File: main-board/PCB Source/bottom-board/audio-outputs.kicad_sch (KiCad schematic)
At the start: 53 parts, among them P11 JACK_TRS_6PINS, P12 JACK_TRS_6PINS, U6 OPA1678IDR, U7 OPA1678IDR

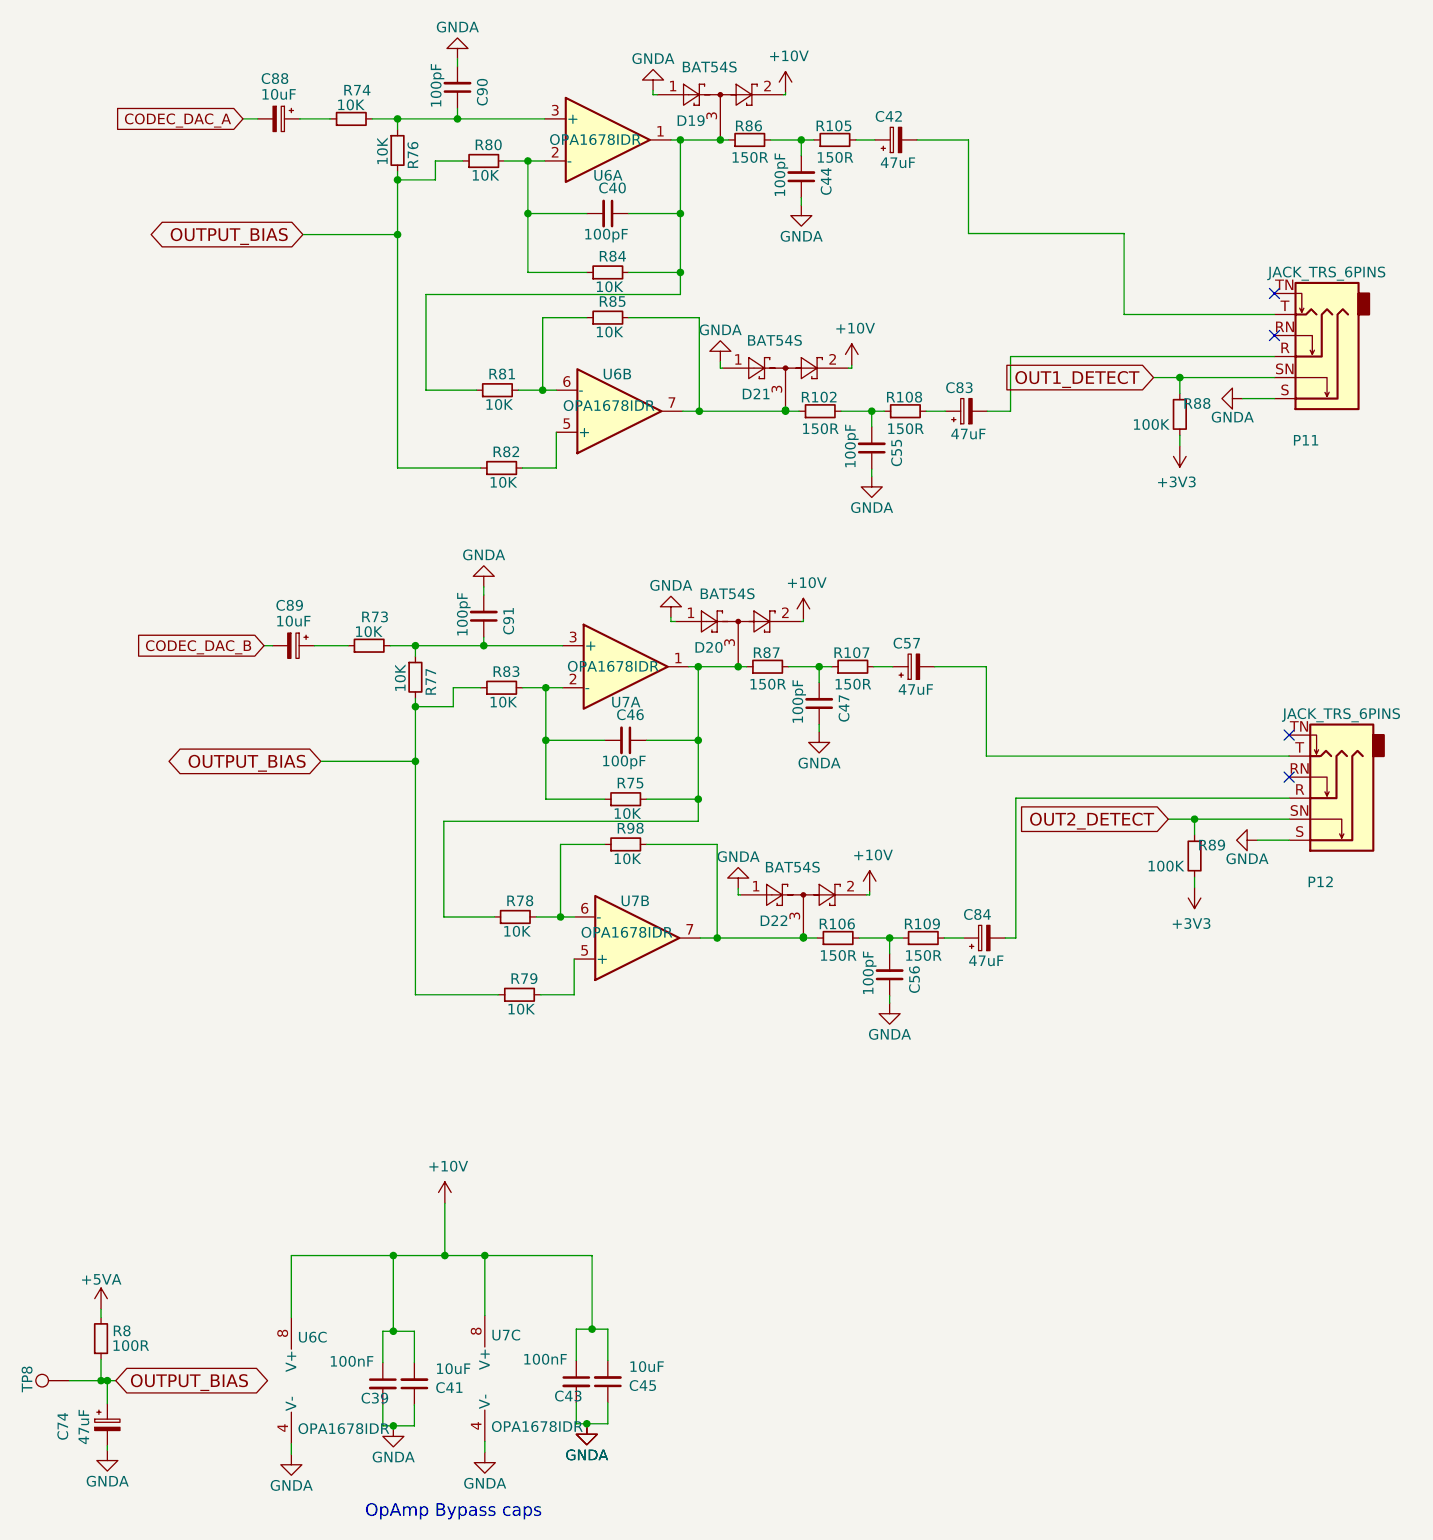
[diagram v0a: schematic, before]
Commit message: mainboard: add bias buffer, update MPNs, clean schematic
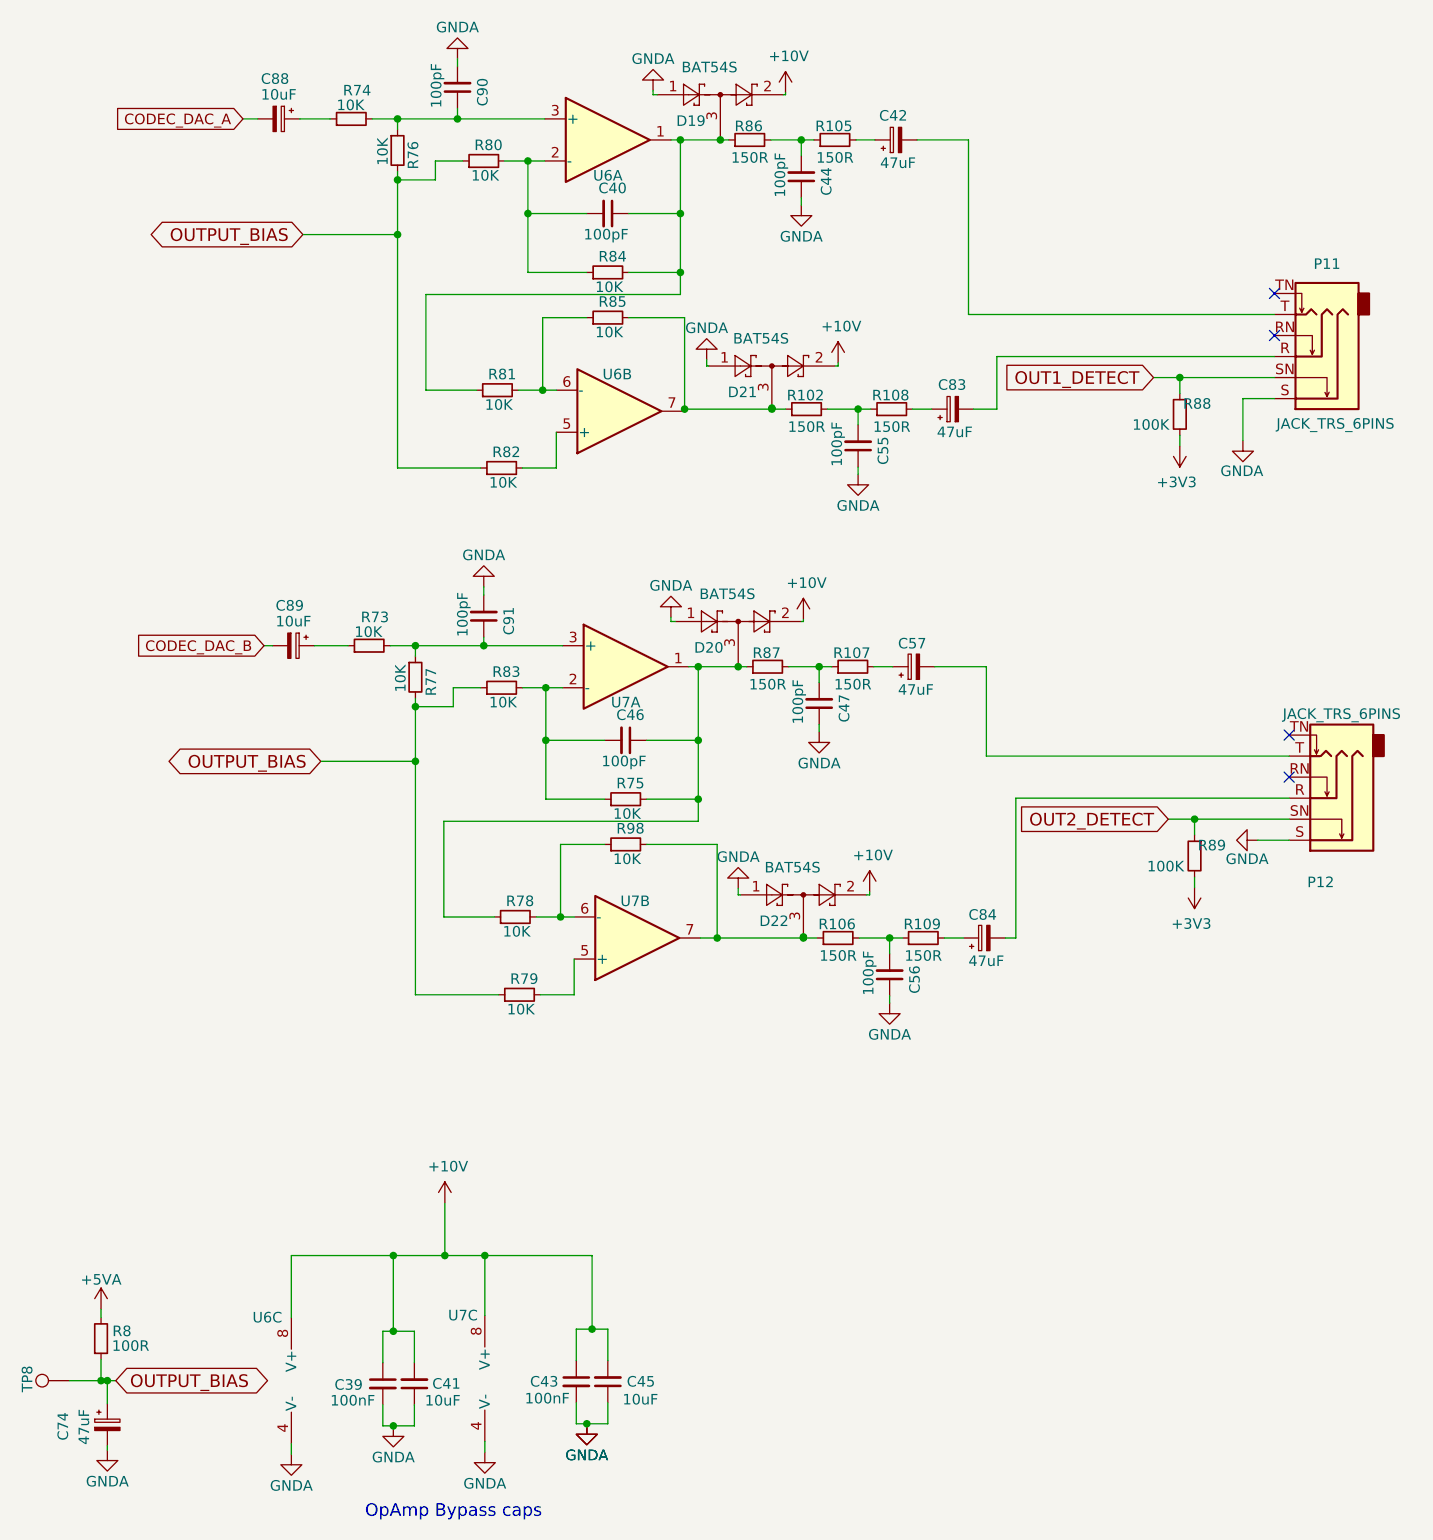
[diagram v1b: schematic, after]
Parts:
- U6, U7: value OPA1678IDR -> (none); footprint Package_SO:SOIC-8_3.9x4.9mm_P1.27mm -> (none)
- U6: value OPA1678IDR -> (none); footprint Package_SO:SOIC-8_3.9x4.9mm_P1.27mm -> (none); MPN (none) -> OPA1678IDR
- U6, U7: value OPA1678IDR -> (none); footprint Package_SO:SOIC-8_3.9x4.9mm_P1.27mm -> (none); MPN LM833DT -> OPA1678IDR
- U7: value OPA1678IDR -> (none); footprint Package_SO:SOIC-8_3.9x4.9mm_P1.27mm -> (none); MPN TL082CDR -> OPA1678IDR
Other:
- moved on the sheet: C55, C83, D21, R102, R108

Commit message: mainboard: modify silkscreen
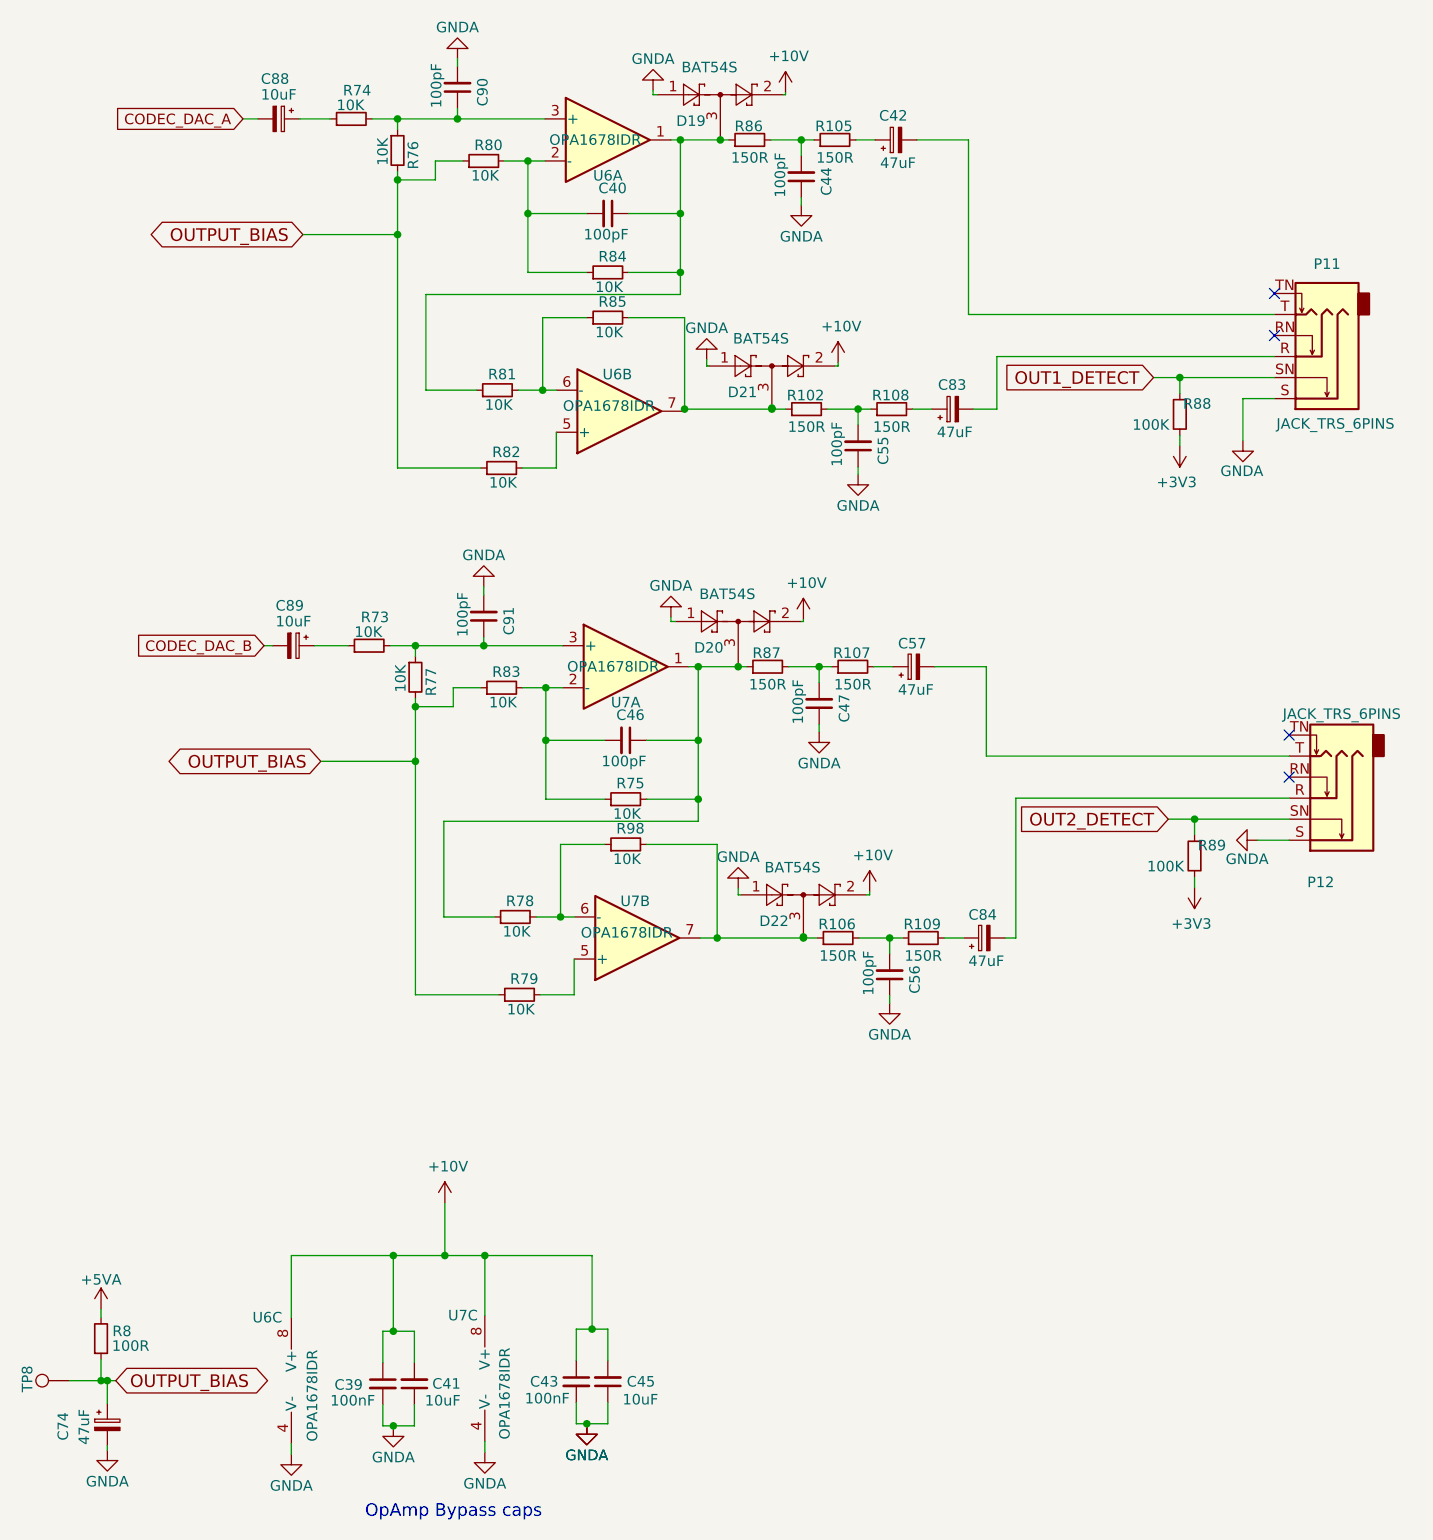
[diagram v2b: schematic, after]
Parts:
- U6, U7: value (none) -> OPA1678IDR; footprint (none) -> Package_SO:SOIC-8_3.9x4.9mm_P1.27mm
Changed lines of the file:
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@@
     (in_bom yes) (on_board yes)
     (property "Reference" "U6" (id 0) (at 89.535 33.909 0))
-    (property "Value" "" (id 1) (at 88.011 29.591 0))
-    (property "Footprint" "" (id 2) (at 89.535 29.591 0)
+    (property "Value" "OPA1678IDR" (id 1) (at 88.011 29.591 0))
+    (property "Footprint" "Package_SO:SOIC-8_3.9x4.9mm_P1.27mm" (id 2) (at 89.535 29.591 0)
       (effects (font (size 1.27 1.27)) hide)
     )
@@
       (effects (font (size 1.27 1.27)) (justify left))
     )
-    (property "Value" "" (id 1) (at 53.848 186.817 90)
-      (effects (font (size 1.27 1.27)) (justify left))
-    )
-    (property "Footprint" "" (id 2) (at 53.848 179.451 0)
+    (property "Value" "OPA1678IDR" (id 1) (at 53.848 186.817 90)
+      (effects (font (size 1.27 1.27)) (justify left))
+    )
+    (property "Footprint" "Package_SO:SOIC-8_3.9x4.9mm_P1.27mm" (id 2) (at 53.848 179.451 0)
       (effects (font (size 1.27 1.27)) hide)
     )
@@
       (effects (font (size 1.27 1.27)) (justify left))
     )
-    (property "Value" "" (id 1) (at 77.089 186.563 90)
-      (effects (font (size 1.27 1.27)) (justify left))
-    )
-    (property "Footprint" "" (id 2) (at 77.216 179.197 0)
+    (property "Value" "OPA1678IDR" (id 1) (at 77.089 186.563 90)
+      (effects (font (size 1.27 1.27)) (justify left))
+    )
+    (property "Footprint" "Package_SO:SOIC-8_3.9x4.9mm_P1.27mm" (id 2) (at 77.216 179.197 0)
       (effects (font (size 1.27 1.27)) hide)
     )
@@
     (in_bom yes) (on_board yes)
     (property "Reference" "U6" (id 0) (at 90.678 57.912 0))
-    (property "Value" "" (id 1) (at 89.662 61.722 0))
-    (property "Footprint" "" (id 2) (at 90.932 62.357 0)
+    (property "Value" "OPA1678IDR" (id 1) (at 89.662 61.722 0))
+    (property "Footprint" "Package_SO:SOIC-8_3.9x4.9mm_P1.27mm" (id 2) (at 90.932 62.357 0)
       (effects (font (size 1.27 1.27)) hide)
     )
@@
     (in_bom yes) (on_board yes)
     (property "Reference" "U7" (id 0) (at 91.694 97.536 0))
-    (property "Value" "" (id 1) (at 90.17 93.218 0))
-    (property "Footprint" "" (id 2) (at 91.694 93.218 0)
+    (property "Value" "OPA1678IDR" (id 1) (at 90.17 93.218 0))
+    (property "Footprint" "Package_SO:SOIC-8_3.9x4.9mm_P1.27mm" (id 2) (at 91.694 93.218 0)
       (effects (font (size 1.27 1.27)) hide)
     )
@@
     (in_bom yes) (on_board yes)
     (property "Reference" "U7" (id 0) (at 92.837 121.539 0))
-    (property "Value" "" (id 1) (at 91.821 125.349 0))
-    (property "Footprint" "" (id 2) (at 93.091 125.984 0)
-      (effects (font (size 1.27 1.27)) hide)
-    )
+    (property "Value" "OPA1678IDR" (id 1) (at 91.821 125.349 0))
+    (property "Footprint" "Package_SO:SOIC-8_3.9x4.9mm_P1.27mm" (id 2) (at 93.091 125.984 0)
+      (effects (font (size 1.27 1.27)) hide)
+    )
